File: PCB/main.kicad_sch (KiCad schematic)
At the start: 51 parts, among them J1 S20B-PADSS-1, J2 S20B-PADSS-1, J3 SWD, SW1 SPST, U1 LM2596-5.0, U2 XC6206P33, U3 MCP2558FD, U4 MCP2558FD, U5 STM32G0B1, Y1 ${Frequency}

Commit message: Add fuse holder
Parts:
- added F1: Fuse, libdb:CMP-0026, symbol 0 LibDB:Circuit Protection/CMP-0026
- D2: footprint LED_SMD:LED_0402_1005Metric -> LED_SMD:LED_0603_1608Metric
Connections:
- net +BATT: now also F1.1; no longer J1.10 (Pin_10), J2.1 (Pin_1)
- new net JST_10_BAT+: F1.2, J1.10 (Pin_10), J2.1 (Pin_1)
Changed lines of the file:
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@@
   (junction (at 72.39 68.58) (diameter 0) (color 0 0 0 0)
   )
-  (junction (at 139.7 24.13) (diameter 0) (color 0 0 0 0)
+  (junction (at 139.7 36.83) (diameter 0) (color 0 0 0 0)
   )
   (junction (at 113.03 68.58) (diameter 0) (color 0 0 0 0)
@@
   (junction (at 60.96 60.96) (diameter 0) (color 0 0 0 0)
   )
-  (junction (at 139.7 21.59) (diameter 0) (color 0 0 0 0)
-  )
   (junction (at 34.29 140.97) (diameter 0) (color 0 0 0 0)
   )
   (junction (at 241.3 24.13) (diameter 0) (color 0 0 0 0)
   )
+  (junction (at 139.7 24.13) (diameter 0) (color 0 0 0 0)
+  )
   (junction (at 146.05 143.51) (diameter 0) (color 0 0 0 0)
   )
@@
     (stroke (width 0) (type default))
   )
-  (wire (pts (xy 139.7 21.59) (xy 140.97 21.59))
+  (wire (pts (xy 139.7 24.13) (xy 144.78 24.13))
     (stroke (width 0) (type default))
   )
@@
     (stroke (width 0) (type default))
   )
-  (wire (pts (xy 139.7 24.13) (xy 125.73 24.13))
+  (wire (pts (xy 139.7 36.83) (xy 125.73 36.83))
     (stroke (width 0) (type default))
   )
@@
     (stroke (width 0) (type default))
   )
+  (wire (pts (xy 139.7 24.13) (xy 139.7 25.4))
+    (stroke (width 0) (type default))
+  )
   (wire (pts (xy 241.3 24.13) (xy 241.3 27.94))
     (stroke (width 0) (type default))
@@
     (stroke (width 0) (type default))
   )
-  (wire (pts (xy 139.7 25.4) (xy 139.7 24.13))
+  (wire (pts (xy 139.7 38.1) (xy 139.7 36.83))
     (stroke (width 0) (type default))
   )
@@
     (stroke (width 0) (type default))
   )
+  (wire (pts (xy 139.7 22.86) (xy 139.7 24.13))
+    (stroke (width 0) (type default))
+  )
   (wire (pts (xy 127 156.21) (xy 147.32 156.21))
     (stroke (width 0) (type default))
@@
     (stroke (width 0) (type default))
   )
-  (wire (pts (xy 125.73 21.59) (xy 139.7 21.59))
+  (wire (pts (xy 125.73 34.29) (xy 139.7 34.29))
     (stroke (width 0) (type default))
   )
@@
     (stroke (width 0) (type default))
   )
-  (wire (pts (xy 139.7 20.32) (xy 139.7 21.59))
+  (wire (pts (xy 139.7 33.02) (xy 139.7 34.29))
     (stroke (width 0) (type default))
   )
@@
     (stroke (width 0) (type default))
   )
-  (wire (pts (xy 139.7 24.13) (xy 140.97 24.13))
+  (wire (pts (xy 139.7 36.83) (xy 140.97 36.83))
     (stroke (width 0) (type default))
   )
@@
     (effects (font (size 1.27 1.27)) (justify right bottom))
   )
-  (label "JST_09_BAT-" (at 125.73 24.13 0) (fields_autoplaced)
+  (label "JST_09_BAT-" (at 125.73 36.83 0) (fields_autoplaced)
     (effects (font (size 1.27 1.27)) (justify left bottom))
   )
@@
     (effects (font (size 1.27 1.27)) (justify left bottom))
   )
-  (label "JST_10_BAT+" (at 125.73 21.59 0) (fields_autoplaced)
+  (label "JST_10_BAT+" (at 125.73 34.29 0) (fields_autoplaced)
     (effects (font (size 1.27 1.27)) (justify left bottom))
   )
@@
     )
   )
-  (symbol (lib_id "power:Earth") (at 139.7 25.4 0) (unit 1)
+  (symbol (lib_id "power:Earth") (at 139.7 38.1 0) (unit 1)
     (in_bom yes) (on_board yes) (dnp no) (fields_autoplaced)
-    (property "Reference" "#PWR0101" (at 139.7 31.75 0)
+    (property "Reference" "#PWR0101" (at 139.7 44.45 0)
       (effects (font (size 1.27 1.27)) hide)
     )
-    (property "Value" "Earth" (at 139.7 29.21 0)
+    (property "Value" "Earth" (at 139.7 41.91 0)
       (effects (font (size 1.27 1.27)) hide)
     )
-    (property "Footprint" "" (at 139.7 25.4 0)
+    (property "Footprint" "" (at 139.7 38.1 0)
       (effects (font (size 1.27 1.27)) hide)
     )
-    (property "Datasheet" "~" (at 139.7 25.4 0)
+    (property "Datasheet" "~" (at 139.7 38.1 0)
       (effects (font (size 1.27 1.27)) hide)
     )
@@
       (effects (font (size 1.27 1.27)) hide)
     )
-    (property "Value" "+3.3V" (at 241.3 19.05 90)
-      (effects (font (size 1.27 1.27)) (justify left))
+    (property "Value" "+3.3V" (at 241.3 19.05 0)
+      (effects (font (size 1.27 1.27)))
     )
     (property "Footprint" "" (at 241.3 22.86 0)
@@
     )
   )
-  (symbol (lib_id "power:PWR_FLAG") (at 140.97 21.59 270) (unit 1)
+  (symbol (lib_id "power:PWR_FLAG") (at 144.78 24.13 270) (unit 1)
     (in_bom yes) (on_board yes) (dnp no) (fields_autoplaced)
-    (property "Reference" "#FLG0102" (at 142.875 21.59 0)
+    (property "Reference" "#FLG0102" (at 146.685 24.13 0)
       (effects (font (size 1.27 1.27)) hide)
     )
-    (property "Value" "PWR_FLAG" (at 144.78 22.225 90)
+    (property "Value" "PWR_FLAG" (at 148.59 24.765 90)
       (effects (font (size 1.27 1.27)) (justify left))
     )
-    (property "Footprint" "" (at 140.97 21.59 0)
+    (property "Footprint" "" (at 144.78 24.13 0)
       (effects (font (size 1.27 1.27)) hide)
     )
-    (property "Datasheet" "~" (at 140.97 21.59 0)
+    (property "Datasheet" "~" (at 144.78 24.13 0)
       (effects (font (size 1.27 1.27)) hide)
     )
@@
       (effects (font (size 1.27 1.27)))
     )
-    (property "Footprint" "LED_SMD:LED_0402_1005Metric" (at 269.24 40.64 90)
+    (property "Footprint" "LED_SMD:LED_0603_1608Metric" (at 269.24 40.64 90)
       (effects (font (size 1.27 1.27)) hide)
     )
@@
       (effects (font (size 1.27 1.27)) hide)
     )
-    (property "Value" "+3.3V" (at 45.72 157.48 90)
-      (effects (font (size 1.27 1.27)) (justify left))
+    (property "Value" "+3.3V" (at 45.72 157.48 0)
+      (effects (font (size 1.27 1.27)))
     )
     (property "Footprint" "" (at 45.72 161.29 0)
@@
     )
   )
-  (symbol (lib_id "power:+5V") (at 59.69 161.29 0) (unit 1)
+  (symbol (lib_id "0 LibDB:Circuit Protection/CMP-0026") (at 139.7 29.21 0) (unit 1)
     (in_bom yes) (on_board yes) (dnp no) (fields_autoplaced)
+    (property "Reference" "F1" (at 142.24 28.575 0)
+      (effects (font (size 1.27 1.27)) (justify left))
+    )
+    (property "Value" "Fuse" (at 142.24 31.115 0)
+      (effects (font (size 1.27 1.27)) (justify left))
+    )
+    (property "Footprint" "libdb:CMP-0026" (at 137.922 29.21 90)
+      (effects (font (size 1.27 1.27)) hide)
+    )
+    (property "Datasheet" "~" (at 139.7 29.21 0)
+      (effects (font (size 1.27 1.27)) hide)
+    )
+    (property "Manufacturer" "Littelfuse" (at 139.7 29.21 0)
+      (effects (font (size 1.27 1.27)) hide)
+    )
+    (property "MPN" "01530007Z" (at 139.7 29.21 0)
+      (effects (font (size 1.27 1.27)) hide)
+    )
+    (property "Rating" "~" (at 139.7 29.21 0)
+      (effects (font (size 1.27 1.27)) hide)
+    )
+    (property "LCSC" "C206906" (at 139.7 29.21 0) (show_name)
+      (effects (font (size 1.27 1.27)) hide)
+    )
+    (pin "1")
+    (pin "2")
+    (instances
+      (project "main"
+        (path "/4f4cf64f-c95a-4a4a-b388-e87470ab2a3e"
+          (reference "F1") (unit 1)
+        )
+      )
+    )
+  )
+  (symbol (lib_id "power:+5V") (at 59.69 161.29 0) (unit 1)
+    (in_bom yes) (on_board yes) (dnp no)
     (property "Reference" "#PWR0120" (at 59.69 165.1 0)
       (effects (font (size 1.27 1.27)) hide)
@@
     )
   )
-  (symbol (lib_id "power:+BATT") (at 139.7 20.32 0) (unit 1)
+  (symbol (lib_id "power:+BATT") (at 139.7 22.86 0) (unit 1)
     (in_bom yes) (on_board yes) (dnp no) (fields_autoplaced)
-    (property "Reference" "#PWR0115" (at 139.7 24.13 0)
+    (property "Reference" "#PWR0115" (at 139.7 26.67 0)
       (effects (font (size 1.27 1.27)) hide)
     )
-    (property "Value" "+BATT" (at 139.7 16.51 0)
+    (property "Value" "+BATT" (at 139.7 19.05 0)
       (effects (font (size 1.27 1.27)))
     )
-    (property "Footprint" "" (at 139.7 20.32 0)
+    (property "Footprint" "" (at 139.7 22.86 0)
       (effects (font (size 1.27 1.27)) hide)
     )
-    (property "Datasheet" "" (at 139.7 20.32 0)
+    (property "Datasheet" "" (at 139.7 22.86 0)
       (effects (font (size 1.27 1.27)) hide)
     )
@@
     )
   )
-  (symbol (lib_id "power:PWR_FLAG") (at 140.97 24.13 270) (unit 1)
+  (symbol (lib_id "power:PWR_FLAG") (at 140.97 36.83 270) (unit 1)
     (in_bom yes) (on_board yes) (dnp no) (fields_autoplaced)
-    (property "Reference" "#FLG0101" (at 142.875 24.13 0)
+    (property "Reference" "#FLG0101" (at 142.875 36.83 0)
       (effects (font (size 1.27 1.27)) hide)
     )
-    (property "Value" "PWR_FLAG" (at 144.78 24.765 90)
+    (property "Value" "PWR_FLAG" (at 144.78 37.465 90)
       (effects (font (size 1.27 1.27)) (justify left))
     )
-    (property "Footprint" "" (at 140.97 24.13 0)
+    (property "Footprint" "" (at 140.97 36.83 0)
       (effects (font (size 1.27 1.27)) hide)
     )
-    (property "Datasheet" "~" (at 140.97 24.13 0)
+    (property "Datasheet" "~" (at 140.97 36.83 0)
       (effects (font (size 1.27 1.27)) hide)
     )
@@
       (effects (font (size 1.27 1.27)) hide)
     )
-    (property "Value" "+3.3V" (at 45.72 119.38 90)
-      (effects (font (size 1.27 1.27)) (justify left))
+    (property "Value" "+3.3V" (at 45.72 119.38 0)
+      (effects (font (size 1.27 1.27)))
     )
     (property "Footprint" "" (at 45.72 123.19 0)

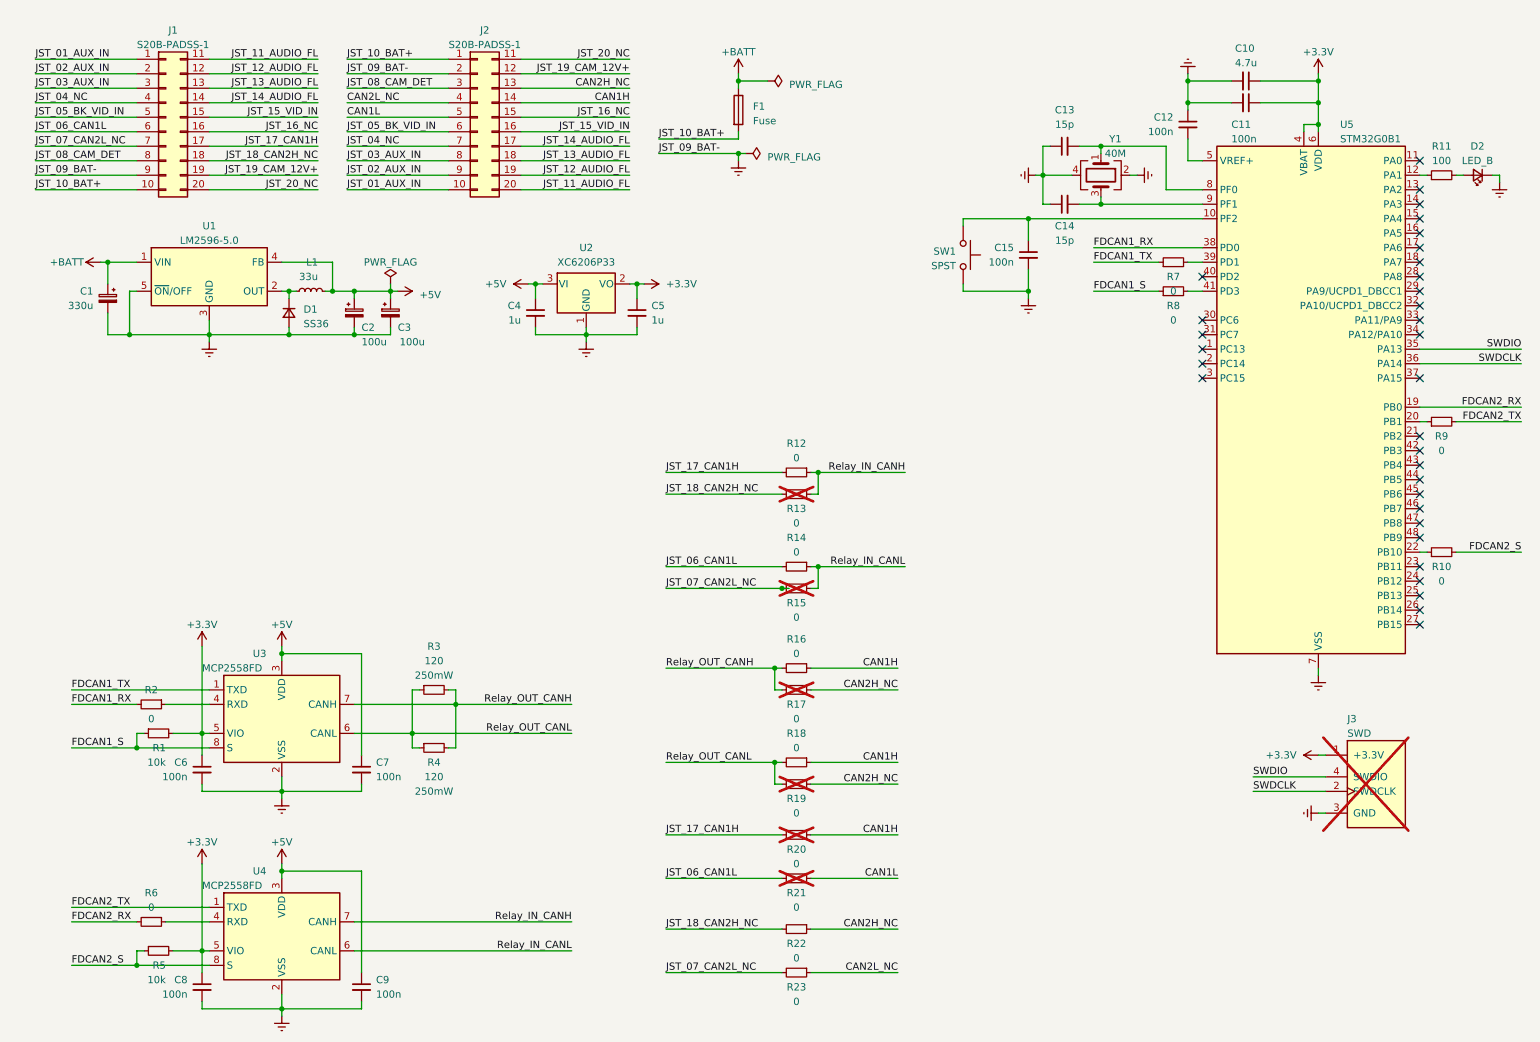
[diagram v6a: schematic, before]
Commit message: Change buck converter
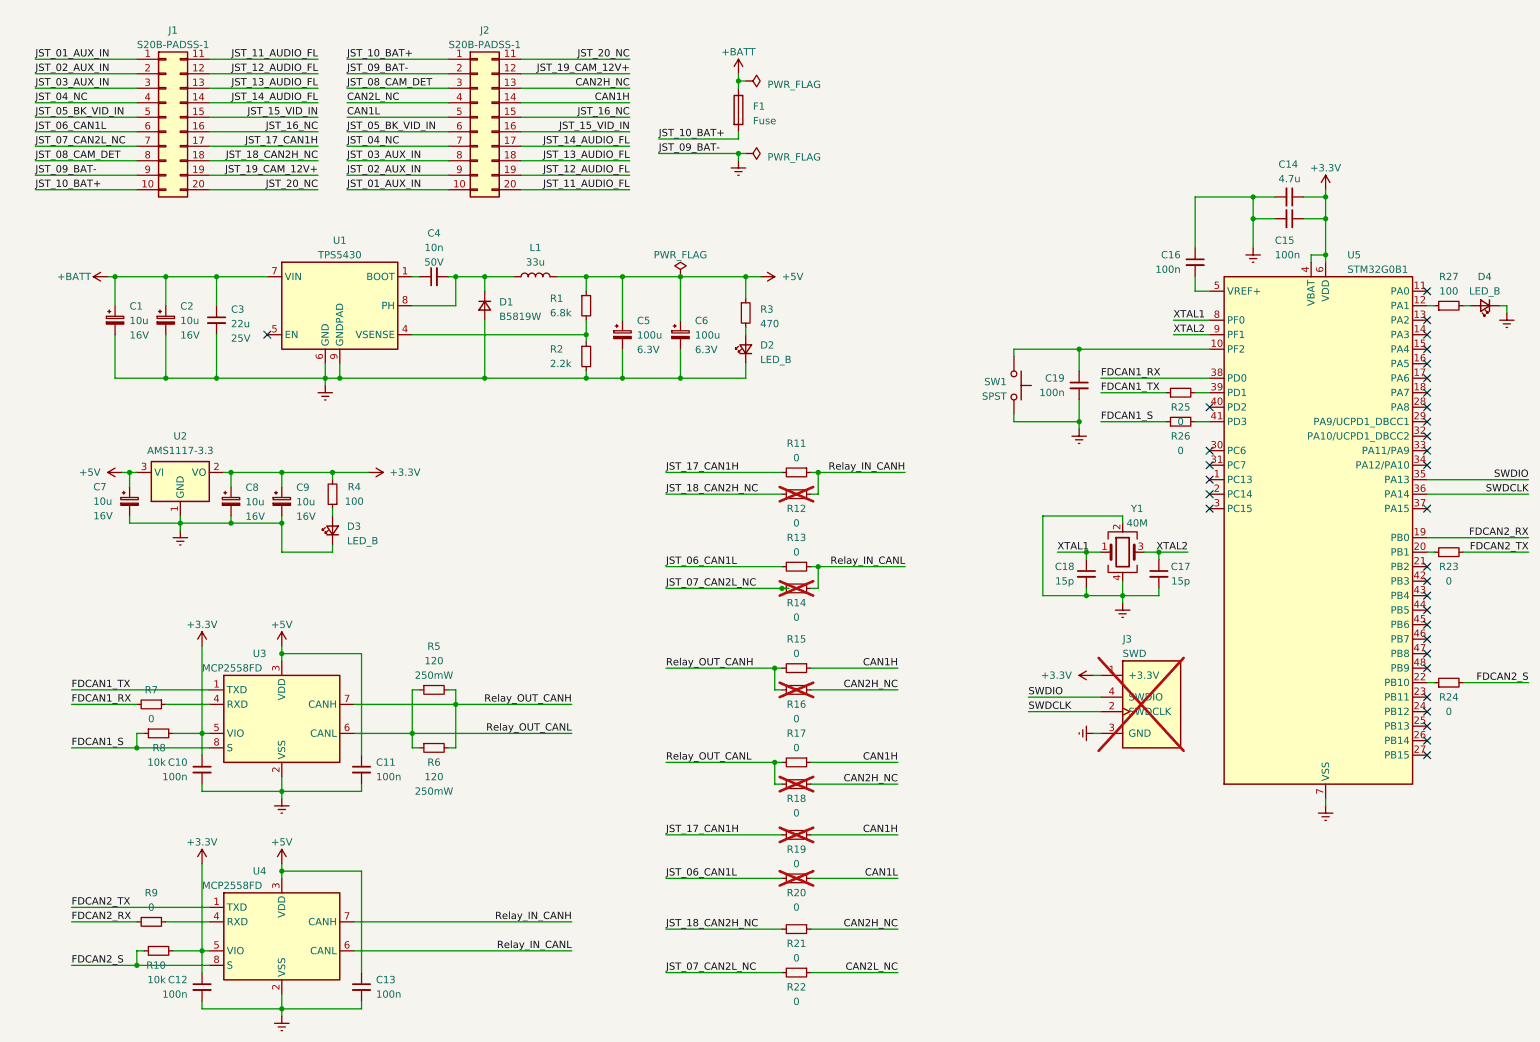
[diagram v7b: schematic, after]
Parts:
- removed C1: ${Capacitance}, Capacitor_SMD:CP_Elec_10x10, symbol 0 LibDB:Capacitors/CMP-0018
- removed C2, C3: ${Capacitance}, Capacitor_Tantalum_SMD:CP_EIA-3528-15_AVX-H, symbol 0 LibDB:Capacitors/CMP-0017
- removed C4, C5: ${Capacitance}, Capacitor_SMD:C_0805_2012Metric, symbol 0 LibDB:Capacitors/CMP-0020
- removed D1: SS36, Diode_SMD:D_SMC, symbol 0 LibDB:Schottky Diodes/CMP-0016
- removed L1: ${Inductance}, Inductor_SMD:L_1210_3225Metric, symbol 0 LibDB:Inductors/CMP-0015
- removed U1: LM2596-5.0, Package_TO_SOT_SMD:TO-263-5_TabPin3, symbol 0 LibDB:DC-DC Converters/CMP-0014
- removed U2: XC6206P33, libdb:CMP-0019, symbol 0 LibDB:LDO Regulators/CMP-0019
- added C1, C2, C7, C8, C9: ${Capacitance}, Capacitor_Tantalum_SMD:CP_EIA-3216-18_Kemet-A, symbol 0 LibDB:Capacitors/CMP-0029
- added C3: ${Capacitance}, Capacitor_SMD:C_1206_3216Metric, symbol 0 LibDB:Capacitors/CMP-0031
- added C4: ${Capacitance}, Capacitor_SMD:C_0402_1005Metric, symbol 0 LibDB:Capacitors/CMP-0032
- added C5, C6: ${Capacitance}, Capacitor_Tantalum_SMD:CP_EIA-3528-15_AVX-H, symbol 0 LibDB:Capacitors/CMP-0017
- added D1: B5819W, Diode_SMD:D_SOD-123, symbol 0 LibDB:Schottky Diodes/CMP-0033
- added D2, D3: LED_B, LED_SMD:LED_0603_1608Metric, symbol 0 LibDB:LEDs/CMP-0023
- added L1: ${Inductance}, libdb:CMP-0036, symbol 0 LibDB:Inductors/CMP-0036
- added R1: ${Resistance}, Resistor_SMD:R_0402_1005Metric, symbol 0 LibDB:Resistors/CMP-0034
- added R2: ${Resistance}, Resistor_SMD:R_0402_1005Metric, symbol 0 LibDB:Resistors/CMP-0035
- added R3: ${Resistance}, Resistor_SMD:R_0402_1005Metric, symbol 0 LibDB:Resistors/CMP-0037
- added R4: ${Resistance}, Resistor_SMD:R_0402_1005Metric, symbol 0 LibDB:Resistors/CMP-0024
- added U1: TPS5430, Package_SO:TI_SO-PowerPAD-8_ThermalVias, symbol 0 LibDB:DC-DC Converters/CMP-0030
- added U2: AMS1117-3.3, Package_TO_SOT_SMD:SOT-223-3_TabPin2, symbol 0 LibDB:LDO Regulators/CMP-0027
- renumbered C6 to C10, C7 to C11, C8 to C12, C9 to C13, C10 to C14, C11 to C15, C12 to C16, C13 to C17, C14 to C18, C15 to C19, D2 to D4, R5 to R10, R12 to R11, R13 to R12, R14 to R13, R15 to R14, R16 to R15, R17 to R16, R18 to R17, R19 to R18, R20 to R19, R21 to R20, R22 to R21, R23 to R22, R9 to R23, R10 to R24, R7 to R25, R8 to R26, R11 to R27, R3 to R5, R4 to R6, R2 to R7, R1 to R8, R6 to R9
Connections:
- net +3.3V: now also C8.1, C9.1, R4.2, U2.2 (VO)
- net +5V: now also C5.1, C6.1, C7.1, L1.2, R1.1, R3.1, U2.3 (VI)
- net +BATT: now also C1.1, C2.1, C3.1, U1.7 (VIN)
- net Earth: now also C17.2, C18.2, C1.2, C2.2, C3.2, C5.2, C6.2, C7.2, C8.2, C9.2, D1.2 (A), D2.1 (K), D3.1 (K), R2.2, U1.6 (GND), U1.9 (GNDPAD), U2.1 (GND); no longer C17.1, C18.1
- net XTAL1: now reaches U5.8 (PF0), Y1.1
- net XTAL1: now also C18.1; no longer C17.2
- net XTAL2: now reaches U5.9 (PF1), Y1.3
- net XTAL2: now also C17.1; no longer C18.2
- new net: R1.2, R2.1, U1.4 (VSENSE)
- new net: C4.2, D1.1 (K), L1.1, U1.8 (PH)
- new net: D3.2 (A), R4.1
- new net: C4.1, U1.1 (BOOT)
- new net: D2.2 (A), R3.2
- no-connect marks 32 -> 33
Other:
- moved on the sheet: C14, C15, C16, C17, C18, C19, D4, J3, R23, R24, R25, R26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

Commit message: Continue development
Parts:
- added ART1: Cat (small, mirrored), libdb:CMP-0044, symbol 0 LibDB:Artwork/CMP-0044
- added ART2: Dog (small), libdb:CMP-0045, symbol 0 LibDB:Artwork/CMP-0045
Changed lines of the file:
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@@
+    )
+  )
+  (symbol (lib_id "0 LibDB:Artwork/CMP-0045") (at 217.17 25.4 0) (unit 1)
+    (in_bom no) (on_board yes) (dnp no) (fields_autoplaced)
+    (property "Reference" "ART2" (at 224.79 24.635 0)
+      (effects (font (size 1.27 1.27)) (justify left))
+    )
+    (property "Value" "Dog (small)" (at 224.79 27.175 0)
+      (effects (font (size 1.27 1.27)) (justify left))
+    )
+    (property "Footprint" "libdb:CMP-0045" (at 217.17 16.51 0)
+      (effects (font (size 1.27 1.27)) hide)
+    )
+    (property "Datasheet" "" (at 217.17 16.51 0)
+      (effects (font (size 1.27 1.27)) hide)
+    )
+    (instances
+      (project "main"
+        (path "/4f4cf64f-c95a-4a4a-b388-e87470ab2a3e"
+          (reference "ART2") (unit 1)
+        )
+      )
     )
   )
@@
         )
       )
+    )
+  )
+  (symbol (lib_id "0 LibDB:Artwork/CMP-0044") (at 180.34 25.4 0) (unit 1)
+    (in_bom no) (on_board yes) (dnp no) (fields_autoplaced)
+    (property "Reference" "ART1" (at 187.96 24.635 0)
+      (effects (font (size 1.27 1.27)) (justify left))
+    )
+    (property "Value" "Cat (small, mirrored)" (at 187.96 27.175 0)
+      (effects (font (size 1.27 1.27)) (justify left))
+    )
+    (property "Footprint" "libdb:CMP-0044" (at 180.34 16.51 0)
+      (effects (font (size 1.27 1.27)) hide)
+    )
+    (property "Datasheet" "" (at 180.34 16.51 0)
+      (effects (font (size 1.27 1.27)) hide)
+    )
+    (instances
+      (project "main"
+        (path "/4f4cf64f-c95a-4a4a-b388-e87470ab2a3e"
+          (reference "ART1") (unit 1)
+        )
+      )
